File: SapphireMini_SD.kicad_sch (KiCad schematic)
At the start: 15 parts, among them J301 503182-1852, U301 MB85RS1MT, U302 TPS22860DBVR

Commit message: Working on update to power controllers
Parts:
- added C303: 100nF, Capacitor_SMD:C_0603_1608Metric, symbol Device:C_Small
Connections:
- net GND: now also C303.2
- net P3V3: now also C303.1
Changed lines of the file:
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@@
   (junction (at 102.87 135.89) (diameter 0) (color 0 0 0 0)
   )
+  (junction (at 62.23 135.89) (diameter 0) (color 0 0 0 0)
+  )
   (junction (at 92.71 81.28) (diameter 0) (color 0 0 0 0)
   )
@@
     (stroke (width 0) (type default) (color 0 0 0 0))
   )
-  (wire (pts (xy 71.12 135.89) (xy 59.69 135.89))
+  (wire (pts (xy 71.12 135.89) (xy 62.23 135.89))
     (stroke (width 0) (type default) (color 0 0 0 0))
   )
@@
     (stroke (width 0) (type default) (color 0 0 0 0))
   )
+  (wire (pts (xy 62.23 135.89) (xy 59.69 135.89))
+    (stroke (width 0) (type default) (color 0 0 0 0))
+  )
   (wire (pts (xy 220.98 62.23) (xy 219.71 60.96))
     (stroke (width 0) (type default) (color 0 0 0 0))
@@
   )
   (wire (pts (xy 199.39 97.79) (xy 199.39 95.25))
+    (stroke (width 0) (type default) (color 0 0 0 0))
+  )
+  (wire (pts (xy 62.23 138.43) (xy 62.23 135.89))
     (stroke (width 0) (type default) (color 0 0 0 0))
   )
@@
     (pin "6")
   )
+  (symbol (lib_id "power:GND") (at 62.23 143.51 0) (mirror y) (unit 1)
+    (in_bom yes) (on_board yes)
+    (property "Reference" "#PWR0307" (id 0) (at 62.23 149.86 0)
+      (effects (font (size 1.27 1.27)) hide)
+    )
+    (property "Value" "GND" (id 1) (at 58.42 144.78 0))
+    (property "Footprint" "" (id 2) (at 62.23 143.51 0)
+      (effects (font (size 1.27 1.27)) hide)
+    )
+    (property "Datasheet" "" (id 3) (at 62.23 143.51 0)
+      (effects (font (size 1.27 1.27)) hide)
+    )
+    (pin "1")
+  )
   (symbol (lib_id "Device:R_US") (at 207.01 73.66 270) (unit 1)
     (in_bom yes) (on_board yes)
@@
       (effects (font (size 1.27 1.27)) hide)
     )
+    (pin "1")
+    (pin "2")
+  )
+  (symbol (lib_id "Device:C_Small") (at 62.23 140.97 0) (unit 1)
+    (in_bom yes) (on_board yes)
+    (property "Reference" "C303" (id 0) (at 64.5668 139.8016 0)
+      (effects (font (size 1.27 1.27)) (justify left))
+    )
+    (property "Value" "100nF" (id 1) (at 64.5668 142.113 0)
+      (effects (font (size 1.27 1.27)) (justify left))
+    )
+    (property "Footprint" "Capacitor_SMD:C_0603_1608Metric" (id 2) (at 62.23 140.97 0)
+      (effects (font (size 1.27 1.27)) hide)
+    )
+    (property "Datasheet" "~" (id 3) (at 62.23 140.97 0)
+      (effects (font (size 1.27 1.27)) hide)
+    )
+    (property "DigiKey Price" "0.10" (id 4) (at 62.23 140.97 0)
+      (effects (font (size 1.27 1.27)) hide)
+    )
+    (property "MPN" "CL05A104KA5NNNC" (id 5) (at 62.23 140.97 0)
+      (effects (font (size 1.27 1.27)) hide)
+    )
+    (property "Manufacturer" "Samsung" (id 6) (at 62.23 140.97 0)
+      (effects (font (size 1.27 1.27)) hide)
+    )
+    (property "Tolerance" "10%" (id 7) (at 62.23 140.97 0)
+      (effects (font (size 1.27 1.27)) hide)
+    )
+    (property "Voltage" "25" (id 8) (at 62.23 140.97 0)
+      (effects (font (size 1.27 1.27)) hide)
+    )
+    (property "Voltage Rating (DC)" "25 volt" (id 9) (at 62.23 140.97 0)
+      (effects (font (size 1.27 1.27)) hide)
+    )
+    (property "Populate" "1" (id 10) (at 62.23 140.97 0)
+      (effects (font (size 1.27 1.27)) hide)
+    )
+    (property "MacroFab_PN" "MF-CAP-0603-0.1uF" (id 11) (at 62.23 140.97 0)
+      (effects (font (size 1.27 1.27)) hide)
+    )
+    (property "Digi-Key_PN" "1276-1006-1-ND " (id 12) (at 62.23 140.97 0)
+      (effects (font (size 1.27 1.27)) hide)
+    )
+    (property "Distributor" "Digikey" (id 13) (at 62.23 140.97 0)
+      (effects (font (size 1.27 1.27)) hide)
+    )
+    (property "DPN" "1276-1006-1-ND " (id 14) (at 62.23 140.97 0)
+      (effects (font (size 1.27 1.27)) hide)
+    )
+    (property "Description" "0.1 µF ±10% 25V Ceramic Capacitor X5R 0402 (1005 Metric)" (id 15) (at 62.23 140.97 0)
+      (effects (font (size 1.27 1.27)) hide)
+    )

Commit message: Checkpoint
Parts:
- removed C301: 22uF, Capacitor_SMD:C_1206_3216Metric, symbol Device:C_Small
- removed R302: 100K, Resistor_SMD:R_0603_1608Metric, symbol Device:R_Small_US
- removed U302: TPS22860DBVR, SOT95P280X145-6N, symbol sapphireMini:TPS22860DBVR
- J301: footprint SapphineMinimal:MOLEX_503182-1852 -> MOLEX_503182-1852
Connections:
- net GND: now also J301.SW (SWITCH); no longer R310.1
- net SD_CD: now also R310.1; no longer J301.SW (SWITCH)
- net SPI_MOSI: no longer J301.3 (CMD), R308.1
- net SPI_SCK: no longer J301.5 (CLK), R309.1
- net SD_OUTPUT_POWER: now reaches C302.1, J301.4 (VDD), R305.2, R306.1, R307.1
- new net: J301.3 (CMD), R308.1
- new net: J301.5 (CLK), R309.1
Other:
- note removed: "Revision 8 Replaced load control with TPS22860"
- note removed: "U401 pullup defaults to power ON SD card with SD_CS pullup. uController pulls pin 3 of U401 down to shutdown SD power completely"
- moved on the sheet: C302, C303, J301, R301, R303, R304, R305, R306, R307, R308, R309, R310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

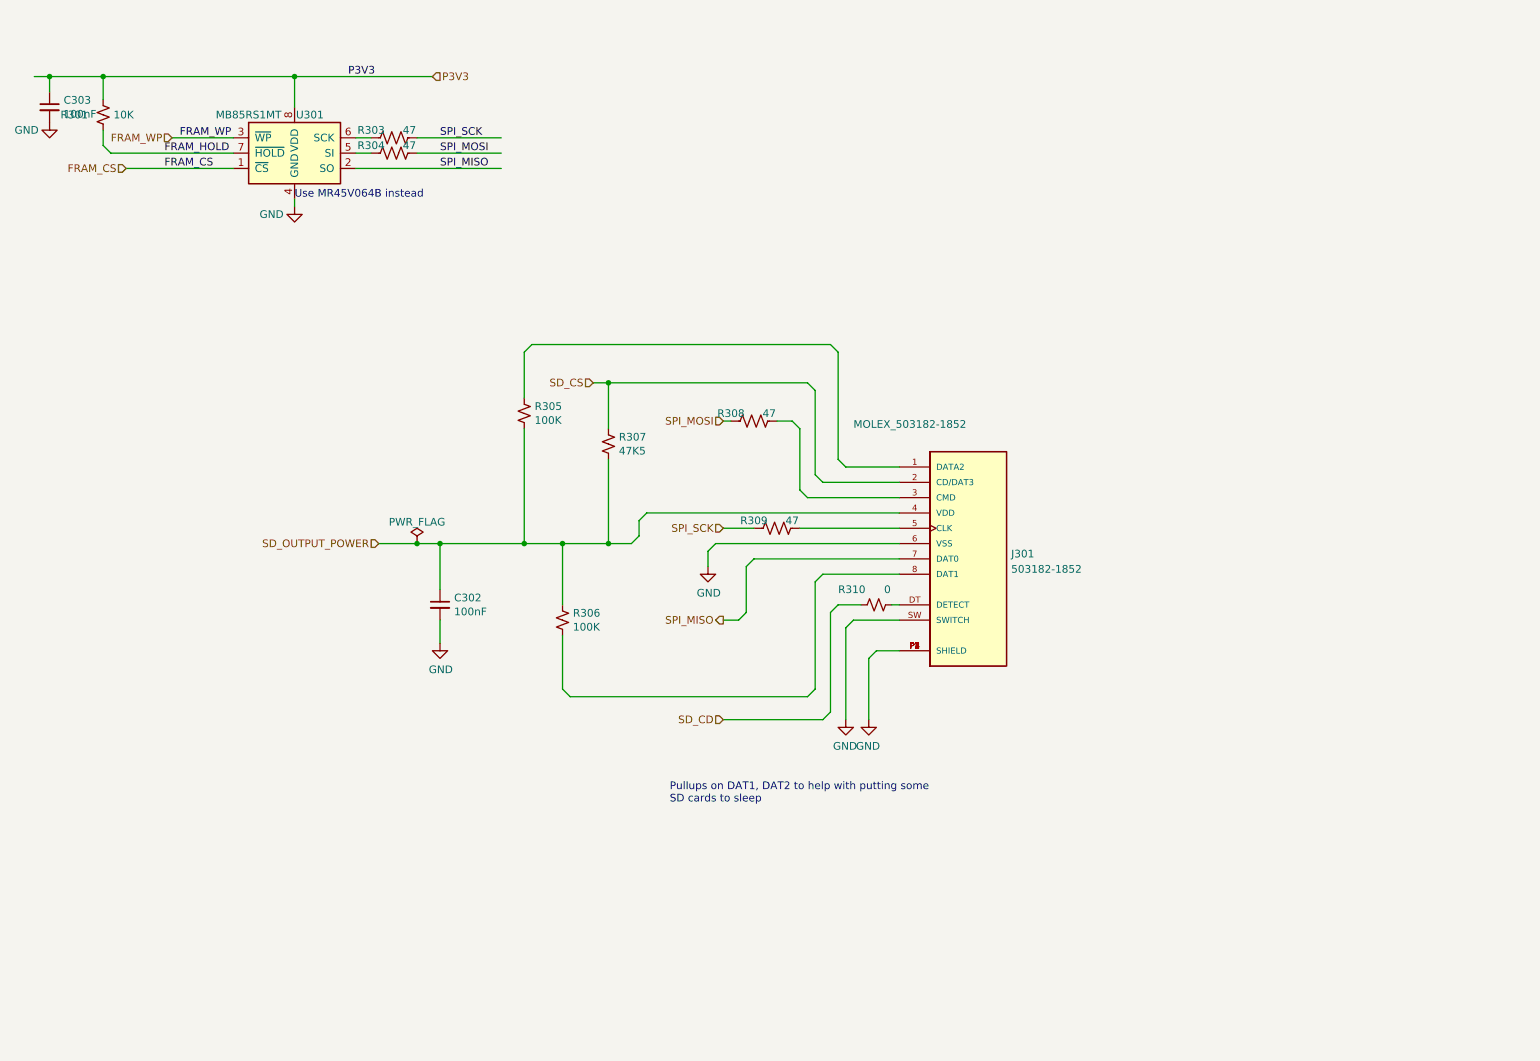
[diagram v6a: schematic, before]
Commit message: Updating for parts avail
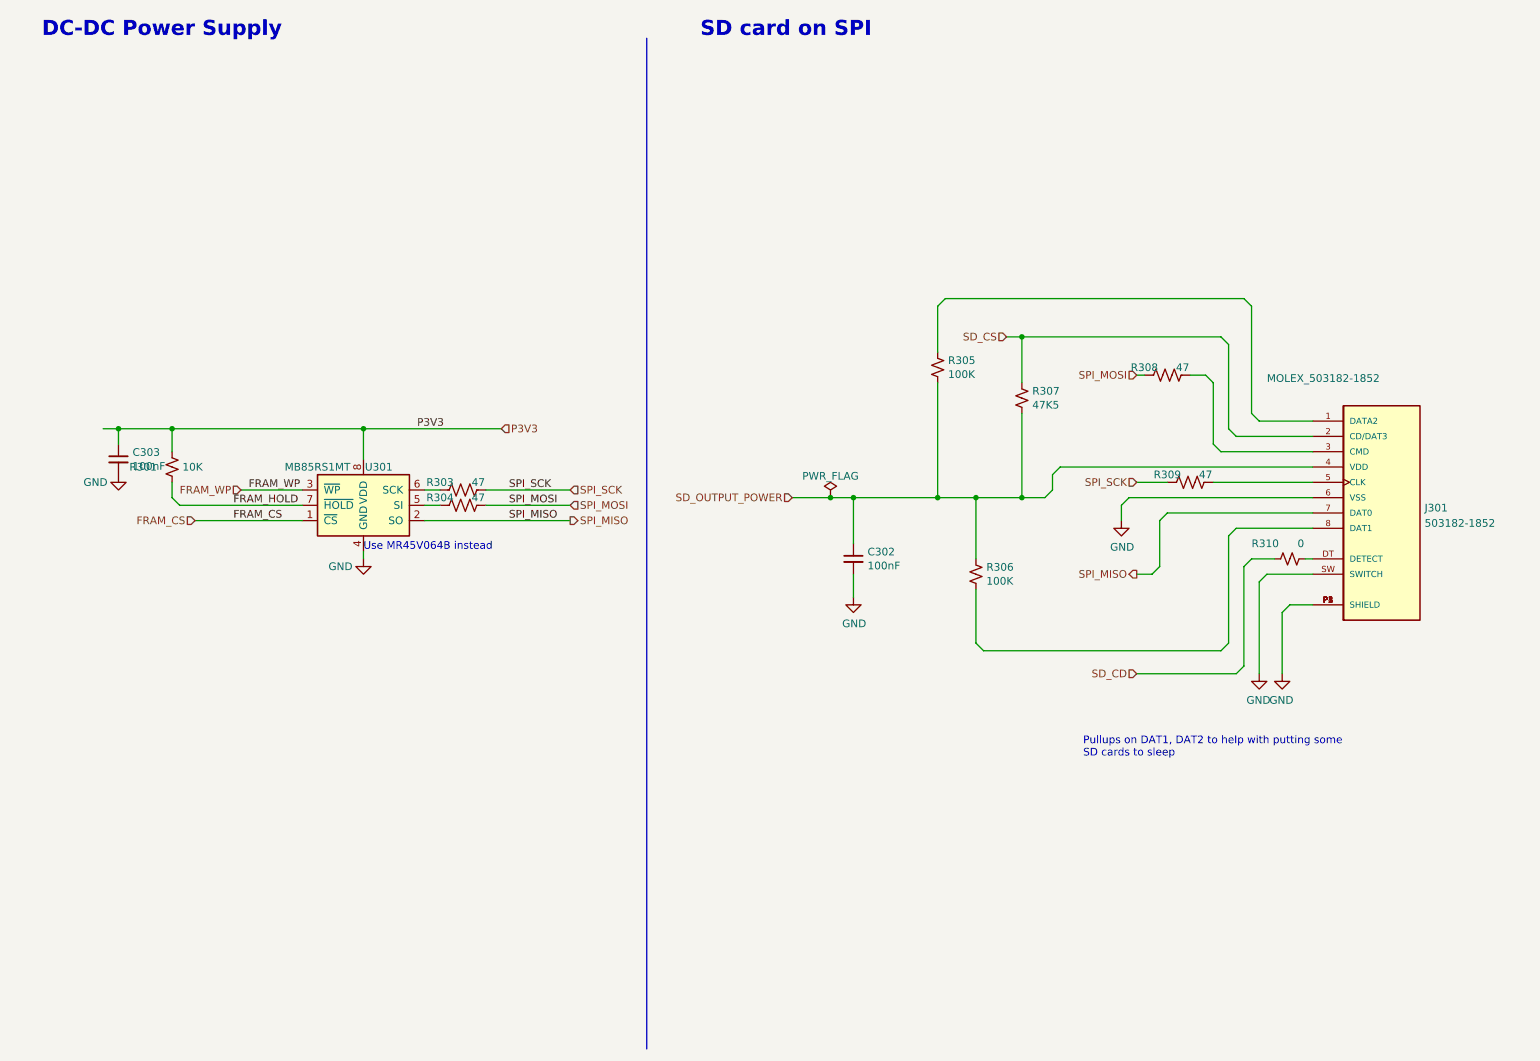
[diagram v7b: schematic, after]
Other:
- note added: "DC-DC Power Supply"
- note added: "SD card on SPI"
- moved on the sheet: C302, C303, J301, R301, R303, R304, R305, R306, R307, R308, R309, R310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
